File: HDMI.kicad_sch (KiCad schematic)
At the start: 6 parts, among them J501 690-019-298-412, U403 TPD4EUSB30, U404 TPD4EUSB30, U405 STMPS2151STR

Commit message: power symbols
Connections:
- net 5V renamed +5V
- net HDMI_5v renamed HDMI_+5V

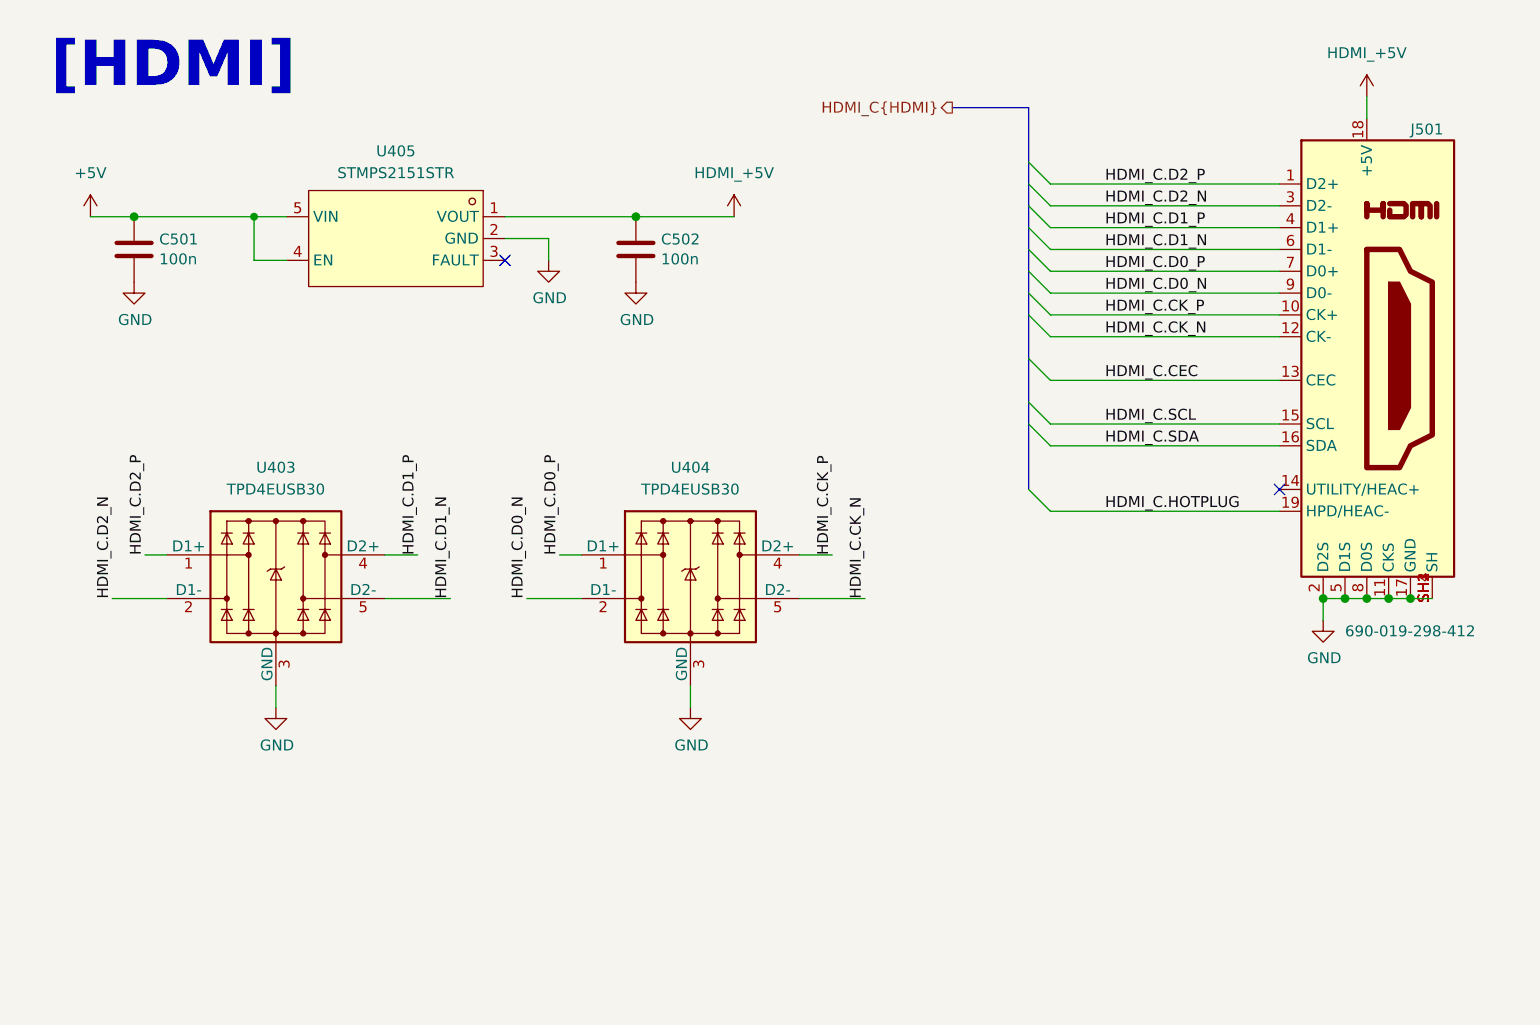
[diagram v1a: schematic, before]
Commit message: esd HDMI complete
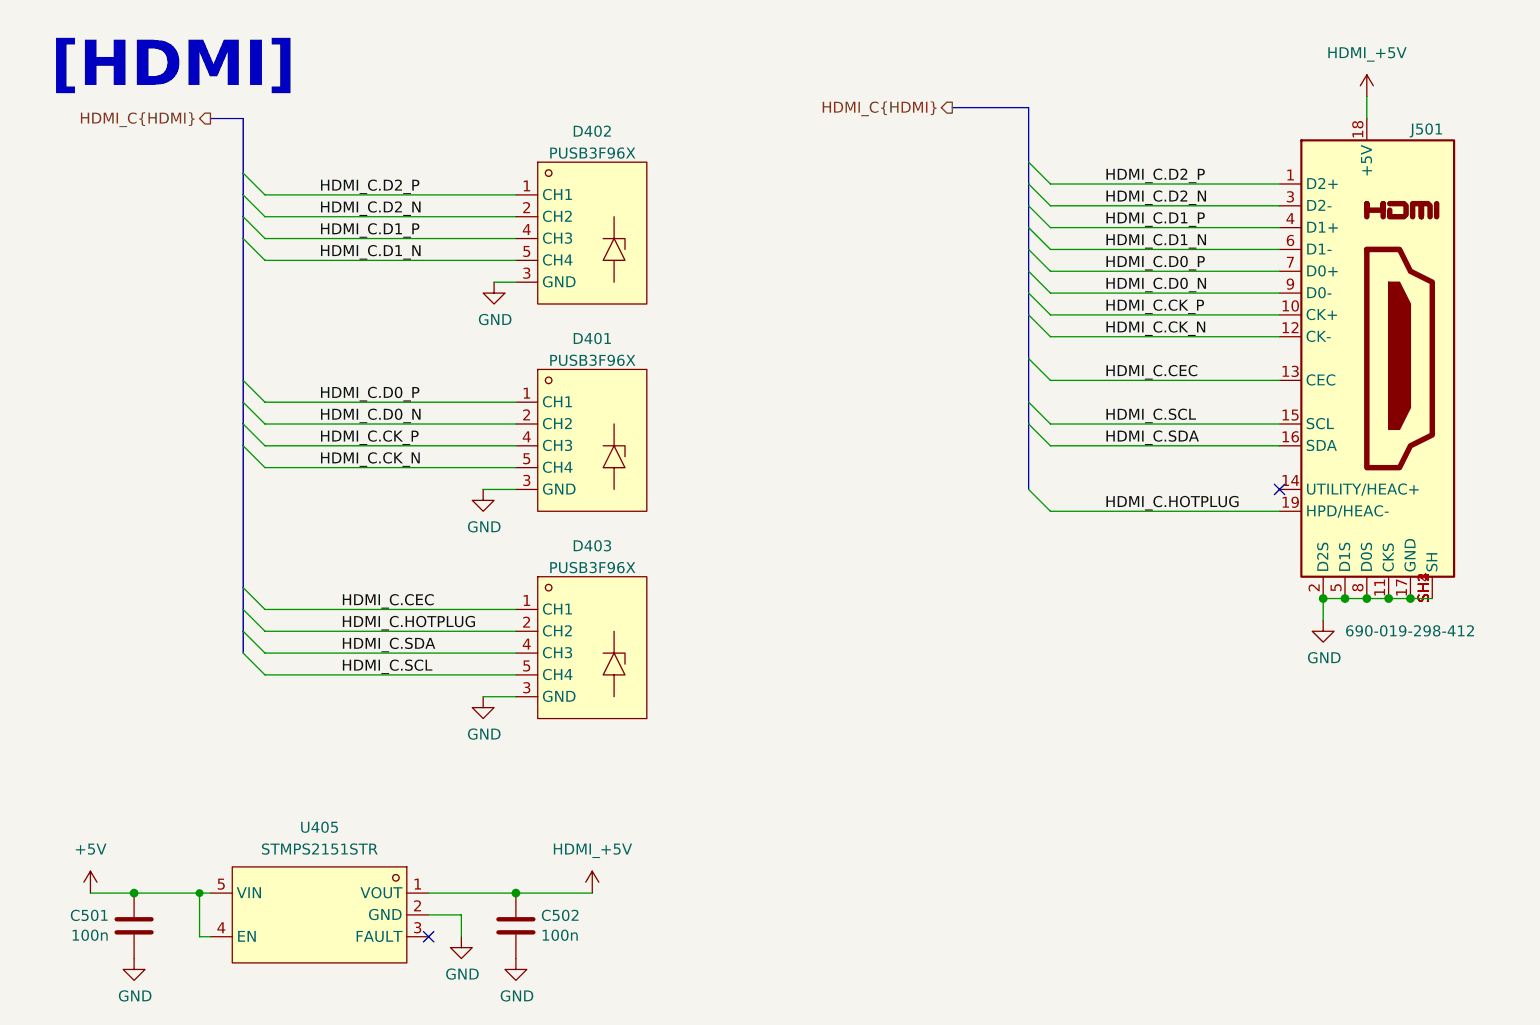
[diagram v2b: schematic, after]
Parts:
- removed U403, U404: TPD4EUSB30, Package_SON:USON-10_2.5x1.0mm_P0.5mm, symbol CM4IO:TPD4EUSB30
- added D401, D402, D403: PUSB3F96X, EasyEDA:DFN2510A-10_L2.5-W1.0-P0.50-BL, symbol EasyEDA:PUSB3F96X
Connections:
- net GND: now also D401.3 (GND), D401.8 (GND), D402.3 (GND), D402.8 (GND), D403.3 (GND), D403.8 (GND)
- net HDMI_C.CEC: now also D403.1 (CH1), D403.10 (NC)
- net HDMI_C.CK_N: now also D401.5 (CH4), D401.6 (NC)
- net HDMI_C.CK_P: now also D401.4 (CH3), D401.7 (NC)
- net HDMI_C.D0_N: now also D401.2 (CH2), D401.9 (NC)
- net HDMI_C.D0_P: now also D401.1 (CH1), D401.10 (NC)
- net HDMI_C.D1_N: now also D402.5 (CH4), D402.6 (NC)
- net HDMI_C.D1_P: now also D402.4 (CH3), D402.7 (NC)
- net HDMI_C.D2_N: now also D402.2 (CH2), D402.9 (NC)
- net HDMI_C.D2_P: now also D402.1 (CH1), D402.10 (NC)
- net HDMI_C.HOTPLUG: now also D403.2 (CH2), D403.9 (NC)
- net HDMI_C.SCL: now also D403.5 (CH4), D403.6 (NC)
- net HDMI_C.SDA: now also D403.4 (CH3), D403.7 (NC)
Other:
- moved on the sheet: C501, C502, U405
